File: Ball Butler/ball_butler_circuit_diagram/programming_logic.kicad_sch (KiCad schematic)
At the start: 14 parts

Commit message: Minor update to schematic
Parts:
- added U?: throw_scheduler, symbol Ball_Butler_Programming_Logic_Symbol_Library:throw_scheduler
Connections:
- net at U?. (Throw_Num): now also U?. (Throw_Num); no longer U?. (Throw_Num)
- new net: U?. (Throw_Num), U?. (Throw_Num)
- new net: U?. (CRC_Result), U?. (Pose_6DoF), U?. (Throw_Num)
- new net: U?. (CRC_Result), U?. (Throw_Num), U?. (Throw_Vel), U?. (Yaw_Angle)
- new net: U?. (Throw_Num), U?. (Throw_Vel)
- new net: U?. (Throw_Vel), U?. (Throw_Vel), U?. (Yaw_Angle)
- new net: U?. (Target_Yaw_Angle), U?. (Yaw_Angle)
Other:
- note added: "- ODrive Error handling? - Command Scheduling"
- note added: "Command ID = 0X7D1 Throw Num reports back the commanded Throw Number (v_x, v_y, v_z) describe the landing state of the ball and allows Jugglebot to orient itself correctly. These values are 0.2 mm/LSB, giving a max value of ~13.1 m/s Checksum: CRC16 (int16) requires CRC-16/CCITT-FALSE over `Throw Command` data (bytes 0–7) [Allows Jugglebot to confirm catch vel pairing with throw command. Redundan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"
- note removed: "- ODrive Error handling?"
- note removed: "Command ID = 0X7D1 Throw Num reports back the commanded Throw Number (v_x, v_y, v_z) describe the landing state of the ball and allows Jugglebot to orient itself correctly. These values are 0.2 mm/LSB, giving a max value of ~13.1 m/s Checksum: CRC16 (int16) requires CRC-16/CCITT-FALSE over `Throw Command` data (bytes 0–7) [Allows Jugglebot to confirm catch vel pairing with throw command]"

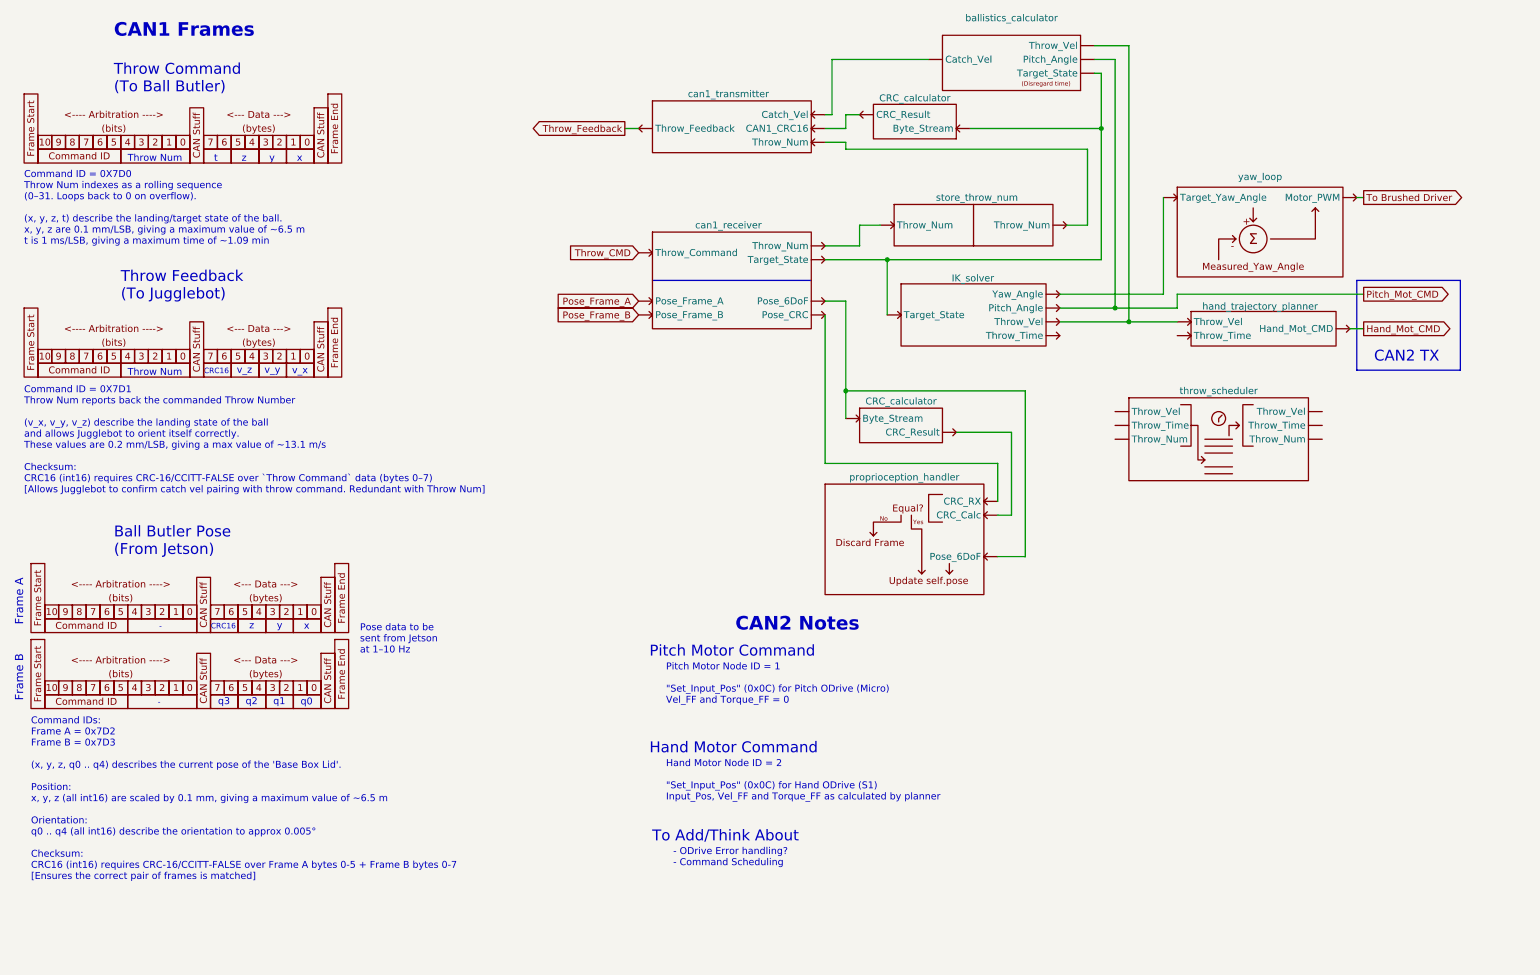
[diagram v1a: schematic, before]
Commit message: Update circuit diagram
Add ROS -> CAN1 = CAN2
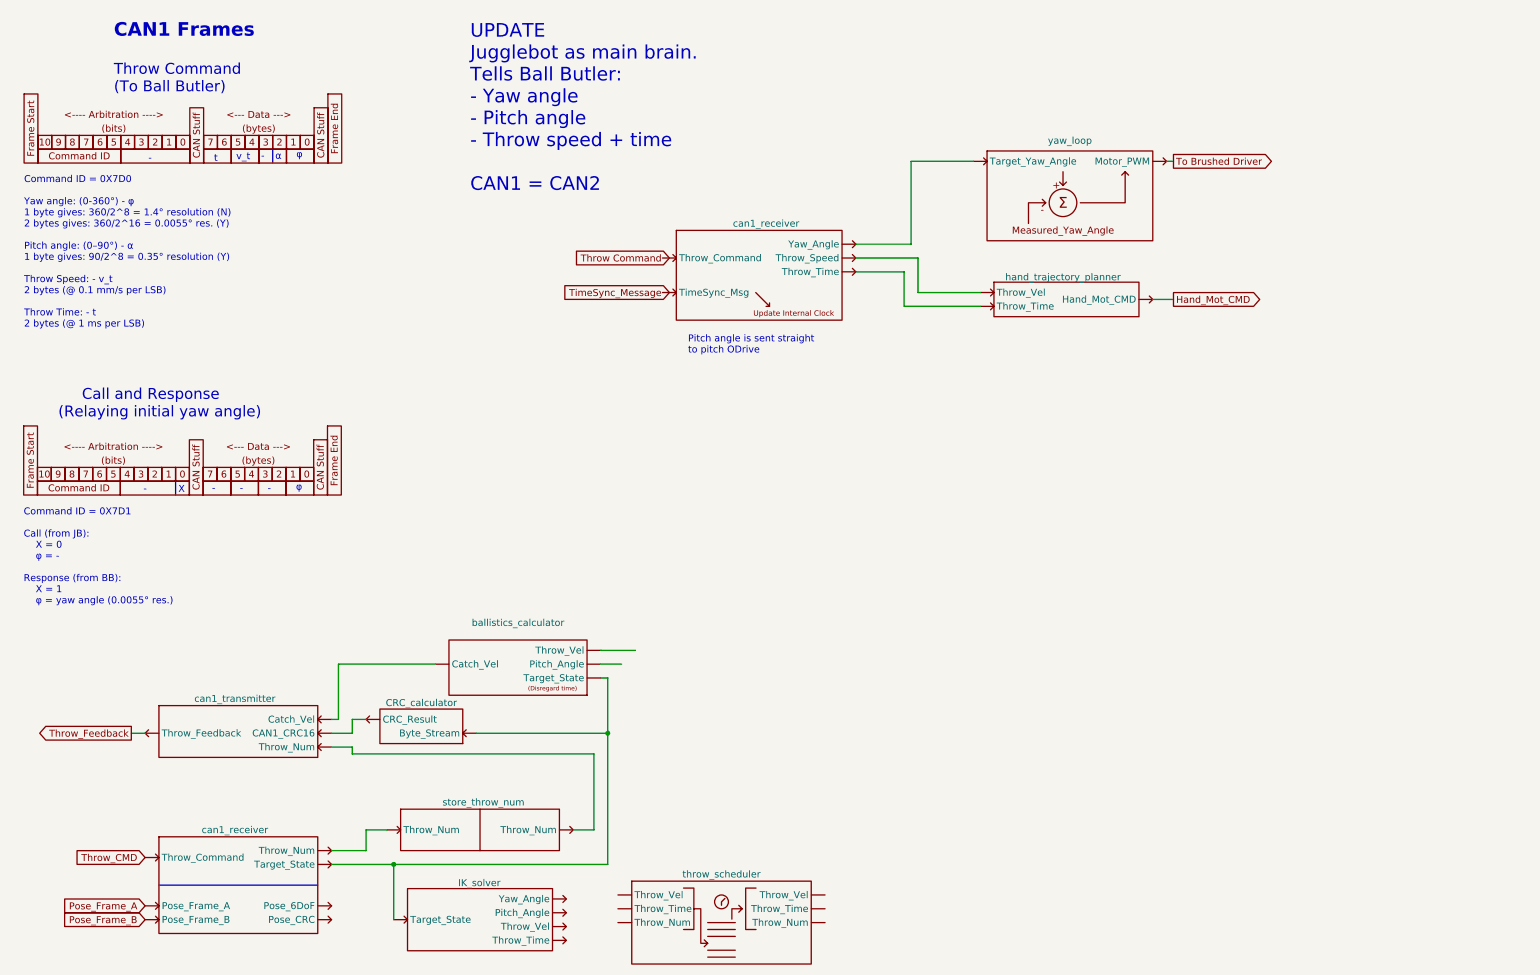
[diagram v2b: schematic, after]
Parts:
- removed U? (x3): CAN_Frame, symbol Ball_Butler_Programming_Logic_Symbol_Library:CAN_Frame
- removed U?: CRC_calculator, symbol Ball_Butler_Programming_Logic_Symbol_Library:CRC_calculator
- removed U?: proprioception_handler, symbol Ball_Butler_Programming_Logic_Symbol_Library:proprioception_handler
- added U?: can1_receiver, symbol Ball_Butler_Programming_Logic_Symbol_Library:can1_receiver
- added U?: CAN_Frame, symbol Ball_Butler_Programming_Logic_Symbol_Library:CAN_Frame
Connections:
- net at U?. (Throw_Num): now also U?. (Throw_Num); no longer U?. (Throw_Num)
- net at U?. (Yaw_Angle): no longer U?. (Target_Yaw_Angle)
- removed net Pitch_Mot_CMD: U?. (Throw_Vel), U?. (Yaw_Angle)
- new net: U?. (Target_Yaw_Angle), U?. (Yaw_Angle)
- new net: U?. (Throw_Vel), U?. (Yaw_Angle) (x2)
- new net: U?. (Throw_Num), U?. (Throw_Num)
- new net: U?. (CRC_Result), U?. (Throw_Num), U?. (Throw_Vel), U?. (Yaw_Angle)
- now unconnected: U?. (Yaw_Angle), U?. (Yaw_Angle)
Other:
- note added: "Call and Response (Relaying initial yaw angle)"
- note added: "Command ID = 0X7D0 Yaw angle: (0-360°) - φ 1 byte gives: 360/2^8 = 1.4° resolution (N) 2 bytes gives: 360/2^16 = 0.0055° res. (Y) Pitch angle: (0–90°) - α 1 byte gives: 90/2^8 = 0.35° resolution (Y) Throw Speed: - v_t 2 bytes (@ 0.1 mm/s per LSB) Throw Time: - t 2 bytes (@ 1 ms per LSB)"
- note added: "Command ID = 0X7D1 Call (from JB): X = 0 φ = - Response (from BB): X = 1 φ = yaw angle (0.0055° res.)"
- note added: "Pitch angle is sent straight to pitch ODrive"
- note added: "UPDATE Jugglebot as main brain. Tells Ball Butler: - Yaw angle - Pitch angle - Throw speed + time CAN1 = CAN2"
- note added: "X"
- note added: "v_t"
- note added: "α"
- note added: "φ"
- note removed: "- ODrive Error handling? - Command Scheduling"
- note removed: "Ball Butler Pose (From Jetson)"
- note removed: "CAN2 Notes"
- note removed: "CAN2 TX"
- note removed: "CRC16"
- note removed: "Command ID = 0X7D0 Throw Num indexes as a rolling sequence (0–31. Loops back to 0 on overflow). (x, y, z, t) describe the landing/target state of the ball. x, y, z are 0.1 mm/LSB, giving a maximum value of ~6.5 m t is 1 ms/LSB, giving a maximum time of ~1.09 min"
- note removed: "Command ID = 0X7D1 Throw Num reports back the commanded Throw Number (v_x, v_y, v_z) describe the landing state of the ball and allows Jugglebot to orient itself correctly. These values are 0.2 mm/LSB, giving a max value of ~13.1 m/s Checksum: CRC16 (int16) requires CRC-16/CCITT-FALSE over `Throw Command` data (bytes 0–7) [Allows Jugglebot to confirm catch vel pairing with throw command. Redundan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"
- note removed: "Command IDs: Frame A = 0x7D2 Frame B = 0x7D3 (x, y, z, q0 .. q4) describes the current pose of the 'Base Box Lid'. Position: x, y, z (all int16) are scaled by 0.1 mm, giving a maximum value of ~6.5 m Orientation: q0 .. q4 (all int16) describe the orientation to approx 0.005° Checksum: CRC16 (int16) requires CRC-16/CCITT-FALSE over Frame A bytes 0-5 + Frame B bytes 0-7 [Ensures the correct pair of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"
- note removed: "Frame A"
- note removed: "Frame B"
- note removed: "Hand Motor Command"
- note removed: "Hand Motor Node ID = 2 "Set_Input_Pos" (0x0C) for Hand ODrive (S1) Input_Pos, Vel_FF and Torque_FF as calculated by planner"
- note removed: "Pitch Motor Command"
- note removed: "Pitch Motor Node ID = 1 "Set_Input_Pos" (0x0C) for Pitch ODrive (Micro) Vel_FF and Torque_FF = 0"
- note removed: "Pose data to be sent from Jetson at 1–10 Hz"
- note removed: "Throw Feedback (To Jugglebot)"
- note removed: "Throw Num"
- note removed: "To Add/Think About"
- note removed: "q0"
- note removed: "q1"
- note removed: "q2"
- note removed: "q3"
- note removed: "v_x"
- note removed: "v_y"
- note removed: "v_z"
- note removed: "x"
- note removed: "y"
- note removed: "z"

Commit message: Update circuit diagram
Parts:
- removed U?: CAN_Frame, symbol Ball_Butler_Programming_Logic_Symbol_Library:CAN_Frame
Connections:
- net Throw Command: now also U?. (Yaw_Angle)
- net TimeSync_Message: now also U?. (Yaw_Angle)
- net at U?. (Throw_Num): now also U?. (Throw_Num); no longer U?. (Throw_Num)
- net at U?. (Throw_Vel): now also U?. (Throw_Num)
- new net: U?. (Target_Yaw_Angle), U?. (Yaw_Angle)
- new net: U?. (Throw_Vel), U?. (Yaw_Angle) (x2)
- new net: U?. (Throw_Num), U?. (Throw_Num)
- new net: U?. (CRC_Result), U?. (Throw_Num), U?. (Throw_Vel), U?. (Yaw_Angle)
- now unconnected: U?. (Yaw_Angle)
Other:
- note added: "Command ID = 0X7D0 Yaw angle: (0-360°) - φ 1 byte gives: 360/2^8 = 1.4° resolution (N) 2 bytes gives: 360/2^16 = 0.0055° res. (Y) Pitch angle: (0–90°) - α 1 byte gives: 90/2^8 = 0.35° resolution (Y) 2 bytes gives: 90/2^16 = 0.00137° res. (Y) Throw Speed: - v_t 2 bytes (@ 0.1 mm/s per LSB) Throw Time: - t 2 bytes (@ 1 ms per LSB)"
- note removed: "Call and Response (Relaying initial yaw angle)"
- note removed: "Command ID = 0X7D0 Yaw angle: (0-360°) - φ 1 byte gives: 360/2^8 = 1.4° resolution (N) 2 bytes gives: 360/2^16 = 0.0055° res. (Y) Pitch angle: (0–90°) - α 1 byte gives: 90/2^8 = 0.35° resolution (Y) Throw Speed: - v_t 2 bytes (@ 0.1 mm/s per LSB) Throw Time: - t 2 bytes (@ 1 ms per LSB)"
- note removed: "Command ID = 0X7D1 Call (from JB): X = 0 φ = - Response (from BB): X = 1 φ = yaw angle (0.0055° res.)"
- note removed: "X"
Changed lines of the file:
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@@
     (stroke (width 0) (type default) (color 0 0 0 0))
-  )
-  (polyline (pts (xy 44.3731 100.4304) (xy 44.3731 102.9704))
-    (stroke (width 0) (type solid) (color 0 0 0 0))
   )
   (wire (pts (xy 169.49 59.3798) (xy 180.92 59.3798))
@@
     (stroke (width 0) (type default) (color 0 0 0 0))
   )
-  (polyline (pts (xy 62.2356 39.3402) (xy 62.2356 41.8802))
-    (stroke (width 0) (type solid) (color 0 0 0 0))
-  )
   (wire (pts (xy 79.4123 168.3721) (xy 79.4123 164.5621))
     (stroke (width 0) (type default) (color 0 0 0 0))
   )
-  (text "α" (at 62.7149 41.5416 0)
+  (text "α" (at 61.5675 41.4698 0)
     (effects (font (size 1.27 1.27)) (justify left bottom))
   )
@@
     (effects (font (size 2.5 2.5) (thickness 0.5) bold) (justify left bottom))
   )
-  (text "X" (at 44.8785 102.7944 0)
-    (effects (font (size 1.27 1.27)) (justify left bottom))
-  )
-  (text "     Call and Response\n(Relaying initial yaw angle)"
-    (at 22.7831 89.0004 0)
-    (effects (font (size 2 2)) (justify left bottom))
-  )
   (text "-" (at 39.37 41.91 0)
     (effects (font (size 1.27 1.27)) (justify left bottom))
   )
-  (text "-" (at 60.102 41.5246 0)
-    (effects (font (size 1.27 1.27)) (justify left bottom))
-  )
   (text "φ" (at 66.5894 41.2454 0)
     (effects (font (size 1.27 1.27)) (justify left bottom))
   )
-  (text "Command ID = 0X7D1\n\nCall (from JB):\n	X = 0\n	φ = -\n\nResponse (from BB):\n	X = 1\n	φ = yaw angle (0.0055° res.)\n"
-    (at 16.4331 123.2904 0)
-    (effects (font (size 1.27 1.27)) (justify left bottom))
-  )
-  (text "-" (at 61.2942 102.686 0)
-    (effects (font (size 1.27 1.27)) (justify left bottom))
-  )
-  (text "-" (at 51.0648 102.6241 0)
-    (effects (font (size 1.27 1.27)) (justify left bottom))
-  )
-  (text "Command ID = 0X7D0\n\nYaw angle: (0-360°) - φ\n1 byte gives: 360/2^8 = 1.4° resolution (N)\n2 bytes gives: 360/2^16 = 0.0055° res. (Y)\n\nPitch angle: (0–90°) - α\n1 byte gives: 90/2^8 = 0.35° resolution (Y)\n\nThrow Speed: - v_t\n2 bytes (@ 0.1 mm/s per LSB)\n\nThrow Time: - t\n2 bytes (@ 1 ms per LSB)"
+  (text "Command ID = 0X7D0\n\nYaw angle: (0-360°) - φ\n1 byte gives: 360/2^8 = 1.4° resolution (N)\n2 bytes gives: 360/2^16 = 0.0055° res. (Y)\n\nPitch angle: (0–90°) - α\n1 byte gives: 90/2^8 = 0.35° resolution (Y)\n2 bytes gives: 90/2^16 = 0.00137° res. (Y)\n\nThrow Speed: - v_t\n2 bytes (@ 0.1 mm/s per LSB)\n\nThrow Time: - t\n2 bytes (@ 1 ms per LSB)"
     (at 16.51 72.39 0)
     (effects (font (size 1.27 1.27)) (justify left bottom))
@@
     (effects (font (size 1.27 1.27)) (justify left bottom))
   )
-  (text "φ" (at 66.5134 102.4065 0)
-    (effects (font (size 1.27 1.27)) (justify left bottom))
-  )
-  (text "-" (at 56.1718 102.655 0)
-    (effects (font (size 1.27 1.27)) (justify left bottom))
-  )
   (text "Pitch angle is sent straight\nto pitch ODrive" (at 138.6209 77.1628 0)
-    (effects (font (size 1.27 1.27)) (justify left bottom))
-  )
-  (text "-" (at 38.4522 102.7479 0)
     (effects (font (size 1.27 1.27)) (justify left bottom))
   )
@@
     )
   )
-  (global_label "TimeSync_Message" (shape input) (at 135.2 65.7298 180) (fields_autoplaced)
-    (effects (font (size 1.27 1.27)) (justify right))
-    (property "Intersheet References" "${INTERSHEET_REFS}" (id 0) (at 115.0674 65.6504 0)
-      (effects (font (size 1.27 1.27)) (justify right) hide)
-    )
-  )
-  (global_label "Throw Command" (shape input) (at 135.2 59.3798 180) (fields_autoplaced)
-    (effects (font (size 1.27 1.27)) (justify right))
-    (property "Intersheet References" "${INTERSHEET_REFS}" (id 0) (at 117.184 59.3004 0)
+  (global_label "TimeSync_Message" (shape input) (at 133.93 65.7298 180) (fields_autoplaced)
+    (effects (font (size 1.27 1.27)) (justify right))
+    (property "Intersheet References" "${INTERSHEET_REFS}" (id 0) (at 113.7974 65.6504 0)
+      (effects (font (size 1.27 1.27)) (justify right) hide)
+    )
+  )
+  (global_label "Throw Command" (shape input) (at 133.93 59.3798 180) (fields_autoplaced)
+    (effects (font (size 1.27 1.27)) (justify right))
+    (property "Intersheet References" "${INTERSHEET_REFS}" (id 0) (at 115.914 59.3004 0)
       (effects (font (size 1.27 1.27)) (justify right) hide)
     )
@@
     (pin "")
   )
-  (symbol (lib_id "Ball_Butler_Programming_Logic_Symbol_Library:CAN_Frame") (at 46.9131 97.8904 0) (unit 1)
-    (in_bom yes) (on_board yes) (fields_autoplaced)
-    (property "Reference" "U?" (id 0) (at 53.2631 92.8104 0)
-      (effects (font (size 1.27 1.27)) hide)
-    )
-    (property "Value" "CAN_Frame" (id 1) (at 45.6336 95.3504 0)
-      (effects (font (size 1.27 1.27)) hide)
-    )
-    (property "Footprint" "" (id 2) (at 40.5631 97.8904 0)
-      (effects (font (size 1.27 1.27)) hide)
-    )
-    (property "Datasheet" "" (id 3) (at 40.5631 97.8904 0)
-      (effects (font (size 1.27 1.27)) hide)
-    )
-  )
   (symbol (lib_id "Ball_Butler_Programming_Logic_Symbol_Library:hand_trajectory_planner") (at 206.32 64.4598 0) (unit 1)

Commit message: Update Ball Butler schematic
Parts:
- removed U?: store_throw_num, symbol Ball_Butler_Programming_Logic_Symbol_Library:store_throw_num
- removed U?: ballistics_calculator, symbol Ball_Butler_Programming_Logic_Symbol_Library:ballistics_calculator
- removed U?: can1_receiver, symbol Ball_Butler_Programming_Logic_Symbol_Library:can1_receiver
- removed U?: can1_transmitter, symbol Ball_Butler_Programming_Logic_Symbol_Library:can1_transmitter
- removed U?: IK_solver, symbol Ball_Butler_Programming_Logic_Symbol_Library:IK_solver
- removed U?: CRC_calculator, symbol Ball_Butler_Programming_Logic_Symbol_Library:CRC_calculator
- removed U?: throw_scheduler, symbol Ball_Butler_Programming_Logic_Symbol_Library:throw_scheduler
- added U?: ball_reloader, symbol Ball_Butler_Programming_Logic_Symbol_Library:ball_reloader
- added U?: Yaw_Proprioception, symbol Ball_Butler_Programming_Logic_Symbol_Library:Yaw_Proprioception
- added U?: proprioception_handler, symbol Ball_Butler_Programming_Logic_Symbol_Library:proprioception_handler
- added U?: can1_transmitter, symbol Ball_Butler_Programming_Logic_Symbol_Library:can1_transmitter
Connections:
- new net: U?. (Reload_Yaw_Angle), U?. (Target_Yaw_Angle), U?. (Yaw_Angle)
- new net: U?. (Measured_Yaw_Angle), U?. (Reload_Yaw_Angle) (x2)
- new net: U?. (Reload_Yaw_Angle), U?. (Throw_Info)
- new net: U?. (Reload_Yaw_Angle), U?. (Throw_Vel)
- new net: U?. (Measured_Yaw_Angle), U?. (Yaw_Angle) (x4)
- new net: U?. (Throw_Vel), U?. (Yaw_Angle) (x2)
- new net: U?. (Measured_Yaw_Angle), U?. (Measured_Yaw_Angle)
- new net: U?. (Measured_Yaw_Angle), U?. (Target_Yaw_Angle)
- new net: U?. (Measured_Yaw_Angle), U?. (Throw_Vel)
- new net Hand_Heartbeat: U?. (Yaw_Angle)
- new net Pitch_Heartbeat: U?. (Yaw_Angle)
- new net Pitch_Mot_CMD: U?. (Reload_Yaw_Angle)
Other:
- note added: "System states 0. BOOT (home all axes, determine whether ball in hand) 1. IDLE (all axes IDLE, awaiting a command. Ball should be in hand) 2. THROWING (command received, proceeding with throw) 3. RELOADING 4. ERROR (eg. no ball in hand after attempting reload)"
- note added: "Throw Feedback: - (Not) Making throw"
- note removed: "Pitch angle is sent straight to pitch ODrive"
